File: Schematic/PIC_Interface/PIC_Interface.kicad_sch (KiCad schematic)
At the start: 28 parts, among them J401 USB, J402 To µTracer, Q401 BSS138, Q402 BSS138, U401 PIC16F884-IP, U402 FT232RL, U403 TLP185, U404 TLP185

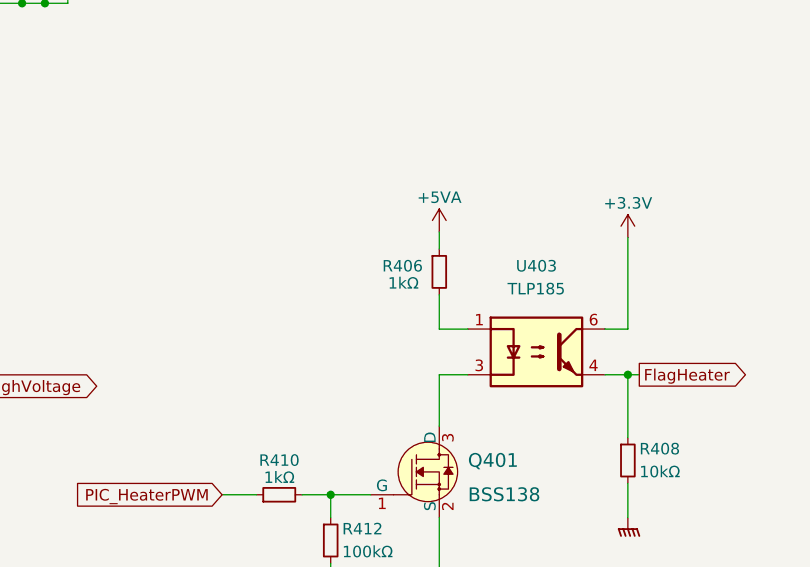
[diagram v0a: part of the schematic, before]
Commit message: Changed component values
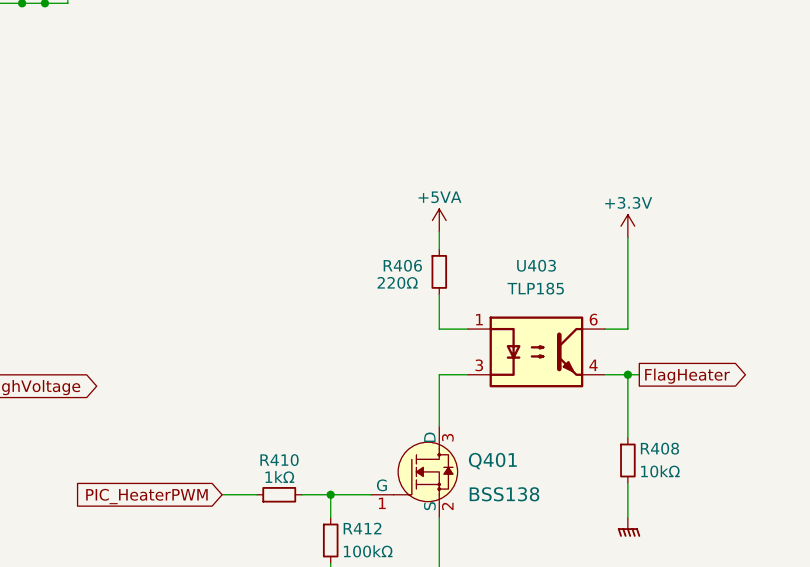
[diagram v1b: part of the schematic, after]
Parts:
- R406: value 1kΩ -> 220Ω
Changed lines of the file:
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@@
       (effects (font (size 1.27 1.27)) (justify left))
     )
-    (property "Value" "1kΩ" (id 1) (at 139.7 149.225 0)
+    (property "Value" "220Ω" (id 1) (at 138.43 149.225 0)
       (effects (font (size 1.27 1.27)) (justify left))
     )
@@
     )
     (path "/45f3a5dc-b360-42e2-850b-9c744f314dff"
-      (reference "R406") (unit 1) (value "1kΩ") (footprint "Resistor_SMD:R_0603_1608Metric_Pad0.98x0.95mm_HandSolder")
+      (reference "R406") (unit 1) (value "220Ω") (footprint "Resistor_SMD:R_0603_1608Metric_Pad0.98x0.95mm_HandSolder")
     )
     (path "/a5fe30a8-d02c-4cfb-874f-ecbe38ddace6"

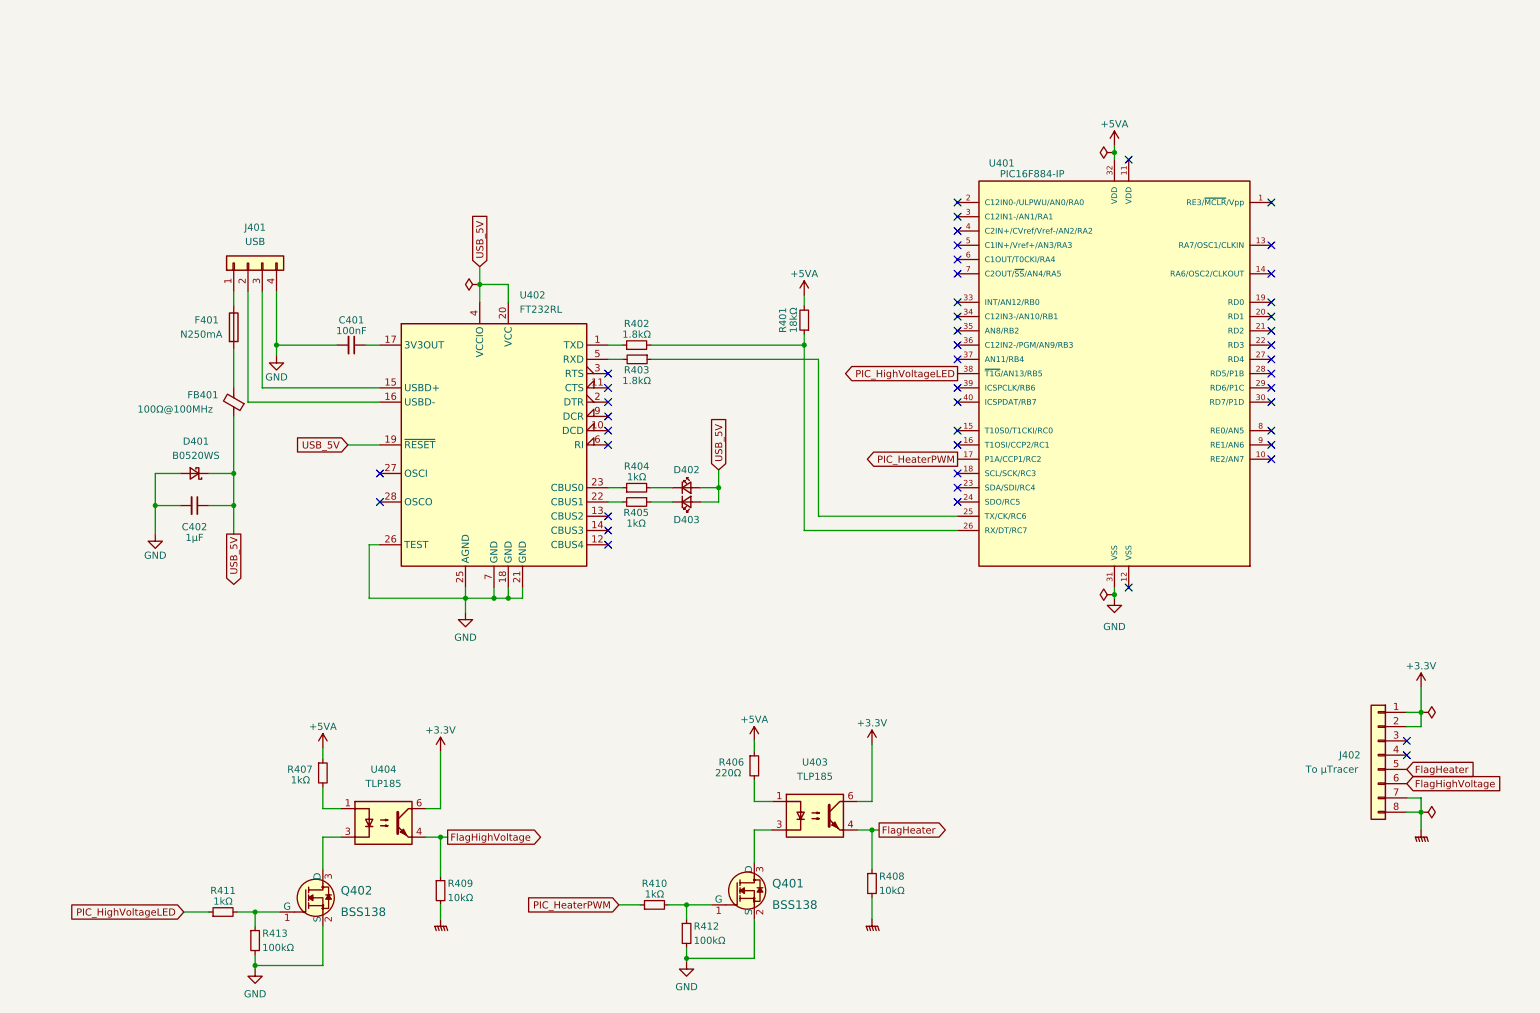
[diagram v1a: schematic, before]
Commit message: Digital heater PSU, first draft
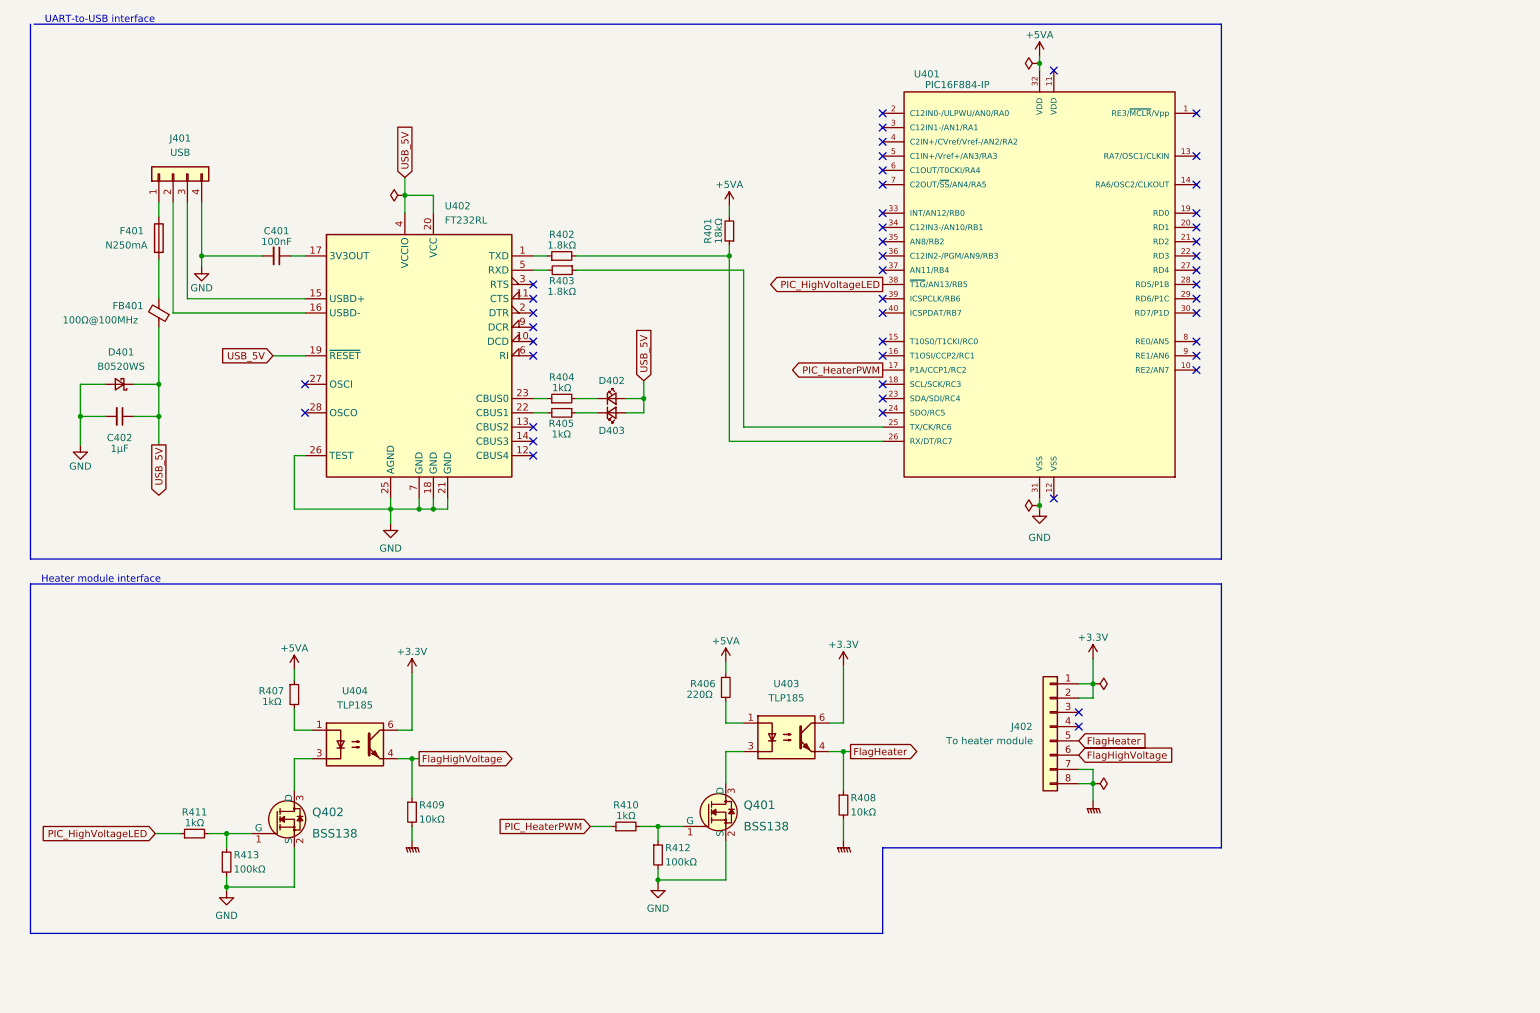
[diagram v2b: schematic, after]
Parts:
- J402: value To µTracer -> To heater module
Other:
- note added: "Heater module interface"
- note added: "UART-to-USB interface"
- moved on the sheet: C401, C402, D401, D402, D403, F401, FB401, J401, J402, Q401, Q402, R401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

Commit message: Added BOM (bill of materials)
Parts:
- U401: value PIC16F884-IP -> Preci-dip 612-87-640-41-001101
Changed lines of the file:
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@@
       (effects (font (size 1.27 1.27)) (justify left))
     )
-    (property "Value" "PIC16F884-IP" (id 1) (at 187.325 26.67 0)
+    (property "Value" "Preci-dip 612-87-640-41-001101" (id 1) (at 187.325 26.67 0)
       (effects (font (size 1.27 1.27)) (justify left))
     )
@@
       (effects (font (size 1.27 1.27) italic) hide)
     )
-    (property "Datasheet" "http://ww1.microchip.com/downloads/en/DeviceDoc/41291D.pdf" (id 3) (at 196.215 62.23 0)
+    (property "Datasheet" "https://no.mouser.com/datasheet/2/571/preci-dip_pdsad00016-22-1746803.pdf" (id 3) (at 196.215 62.23 0)
       (effects (font (size 1.27 1.27)) hide)
     )
@@
     )
     (path "/a670c6d8-0937-4668-95b5-a821d99ebdb0"
-      (reference "U401") (unit 1) (value "PIC16F884-IP") (footprint "myDevices:DIP-40_W15.24mm_Socket_ThroughPCB")
+      (reference "U401") (unit 1) (value "Preci-dip 612-87-640-41-001101") (footprint "myDevices:DIP-40_W15.24mm_Socket_ThroughPCB")
     )
     (path "/a8144e4c-060e-4047-8316-a2581c7e692c"
